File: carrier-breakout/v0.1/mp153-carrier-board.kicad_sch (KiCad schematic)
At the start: 85 parts, among them J1 USB-C_Receptacle_Molex_217179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, J10 3.5mm_Mono_Switched_sm, J11 3.5mm_Mono_Switched_sm, J12 3.5mm_Mono_Switched_sm, J13 3.5mm_Mono_Switched_sm, J2 Eurorack_Power_10pin_Shrouded, J6 Pins_02x40_P2.54mm_TH, J7 Pins_02x40_P2.54mm_TH, U11 TL072H, U12 TL072H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

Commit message: Laying out board - WIP
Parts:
- added JP1, JP10, JP11, JP12, JP13, JP14, JP15, JP2, JP3, JP4, JP5, JP6, JP7, JP8, JP9: SolderJumper_2_Open, 4ms_SolderJumper:JUMPER_SMD_1x2_tiny, symbol 4ms_Net_Tie:SolderJumper_2_Open
- added R1, R2: 10k_0402, 4ms_Resistor:R_0402, symbol 4ms_Resistor_0402:10k_0402
- J6, J7: footprint 4ms_Connector:Pins_2x40_P2.54mm_TH -> Connector_PinHeader_2.54mm:PinHeader_2x40_P2.54mm_Vertical
- R47, R48: value 4.7k_0402 -> 10k_0402; symbol 4ms_Resistor_0402:4.7k_0402 -> 4ms_Resistor_0402:10k_0402; Display 4.7k -> 10k; JLCPCB ID C105871 -> C60490; Part Number RC0402FR-074K7L -> RC0402FR-0710KL; Specifications 4.7k, 1%, 1/16W, 0402 -> 10k, 1%, 1/16W, 0402
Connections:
- net +3V3: now also JP12.2 (B), JP2.1 (A); no longer R47.2, R48.2
- net +5V: now also JP11.2 (B); no longer U3.3 (VDD), U3.4 (VDD)
- net +5VA: now also JP1.1 (A); no longer U9.24 (VCC)
- net A41: now also JP3.1 (A)
- net A43: now also JP4.1 (A)
- net A45: now also JP5.1 (A)
- net A47: now also JP6.1 (A)
- net A49: now also JP7.1 (A)
- net A51: now also JP8.1 (A)
- net A59: now also JP13.2 (B), JP9.1 (A)
- net A61: now also JP10.1 (A), JP14.2 (B)
- net A63: now also JP15.2 (B); no longer U3.5 (INT_N)
- net CODEC_RESET: now also JP3.2 (B)
- net I2C6_SCL: now also R48.2, JP10.2 (B); no longer R47.1, U3.6 (SCL)
- net I2C6_SDA: now also R47.1, JP9.2 (B); no longer R48.1, U3.7 (SDA)
- net SAI_FS: now also JP5.2 (B)
- net SAI_MCLK: now also JP4.2 (B)
- net SAI_SCK: now also JP6.2 (B)
- net SAI_SD_A: now also JP7.2 (B)
- net SAI_SD_B: now also JP8.2 (B)
- net 3v3_CODEC: now reaches C41.1, U9.7 (VDD)
- net 3v3_CODEC: now also R47.2, R48.1, JP2.2 (B)
- new net 3V3_FUSB: JP12.1 (A), R1.2, R2.2
- new net 5VA_CODEC: JP1.2 (B), U9.24 (VCC)
- new net 5V_FUSB: JP11.1 (A), U3.3 (VDD), U3.4 (VDD)
- new net FUSB_I2C6_SCL: JP14.1 (A), R2.1, U3.6 (SCL)
- new net FUSB_I2C6_SDA: JP13.1 (A), R1.1, U3.7 (SDA)
- new net FUSB_INT: JP15.1 (A), U3.5 (INT_N)
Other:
- moved on the sheet: C147, C148, C149, C150, C152, C153, C41, C42, C44, C45, C46, C48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

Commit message: Organized breakoutheader silk
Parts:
- J6, J7: footprint Connector_PinHeader_2.54mm:PinHeader_2x40_P2.54mm_Vertical -> 4ms_Connector:Pins_2x40_P2.54mm_TH

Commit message: WIP - completeing traces
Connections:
- net A71: now also L1.2; no longer L1.1
- net USBSW_5V: now also L1.1; no longer L1.2
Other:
- moved on the sheet: L1
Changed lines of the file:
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@@
 	(symbol
 		(lib_id "4ms_Inductor:FerriteBead_0603_0.8A_300mΩ")
-		(at 403.86 59.69 90)
+		(at 403.86 59.69 270)
+		(mirror x)
 		(unit 1)
 		(exclude_from_sim no)
@@
 		(dnp no)
 		(property "Reference" "L1"
-			(at 404.495 54.61 90)
+			(at 403.225 54.61 90)
 			(effects
 				(font
@@
 		)
 		(property "Footprint" "4ms_Resistor:R_0603"
-			(at 420.37 59.69 0)
+			(at 387.35 59.69 0)
 			(effects
 				(font
@@
 		)
 		(property "Datasheet" "https://datasheet.lcsc.com/lcsc/1811131631_TDK-MPZ1608S102ATA00_C76814.pdf"
-			(at 422.91 59.69 0)
+			(at 384.81 59.69 0)
 			(effects
 				(font
@@
 		)
 		(property "Manufacturer" "TDK"
-			(at 417.83 59.69 0)
+			(at 389.89 59.69 0)
 			(effects
 				(font
@@
 		)
 		(property "Part Number" "MPZ1608S102ATA00"
-			(at 415.29 57.15 0)
+			(at 392.43 57.15 0)
 			(effects
 				(font
@@
 		)
 		(property "Specifications" "Ferrite Bead 0.8A 300mΩ 0603"
-			(at 421.64 59.69 0)
+			(at 386.08 59.69 0)
 			(effects
 				(font
@@
 		)
 		(property "JLCPCB ID" "C76814"
-			(at 425.45 59.69 0)
+			(at 382.27 59.69 0)
 			(effects
 				(font
@@
 		)
 		(property "Production Stage" "A"
-			(at 420.37 62.23 0)
+			(at 387.35 62.23 0)
 			(effects
 				(font

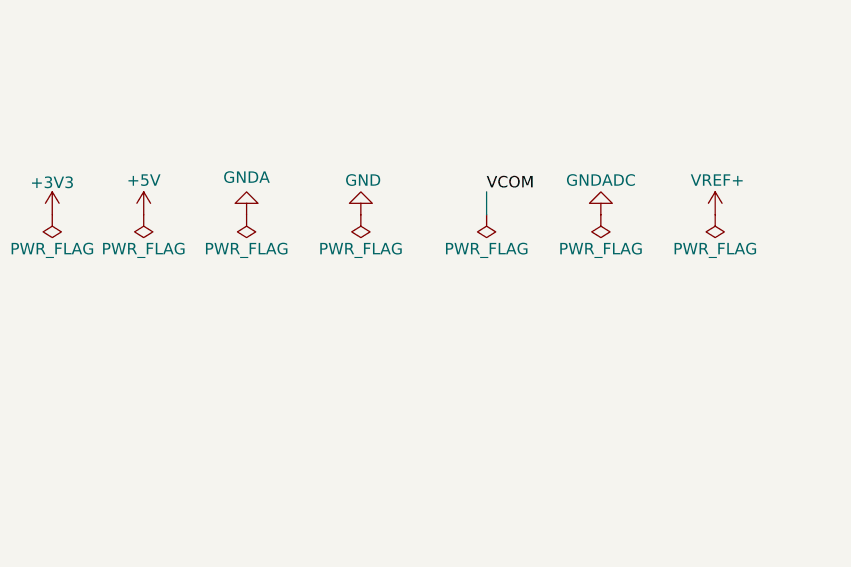
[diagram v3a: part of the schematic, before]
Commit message: Resolved ERC and DRC errors - warnings need to be reviewed. Cleaned up silk and cleaned up Audio out opamp section
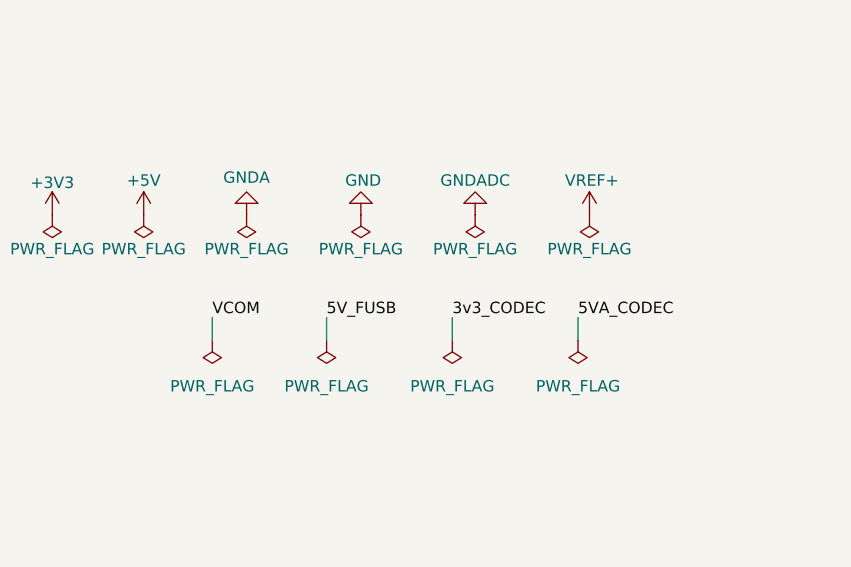
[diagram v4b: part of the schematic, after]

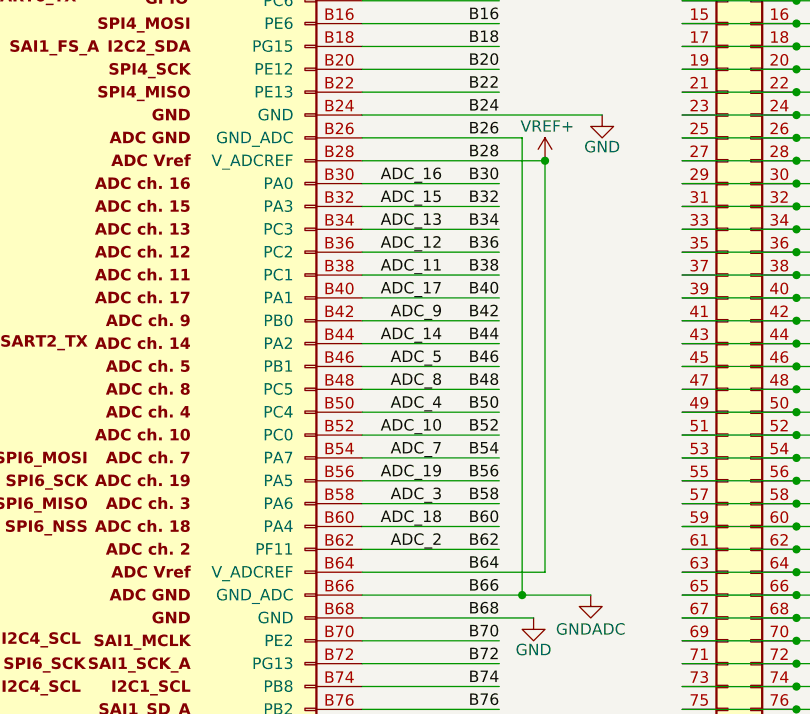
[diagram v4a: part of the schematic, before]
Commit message: Removed redundant ADC net labels
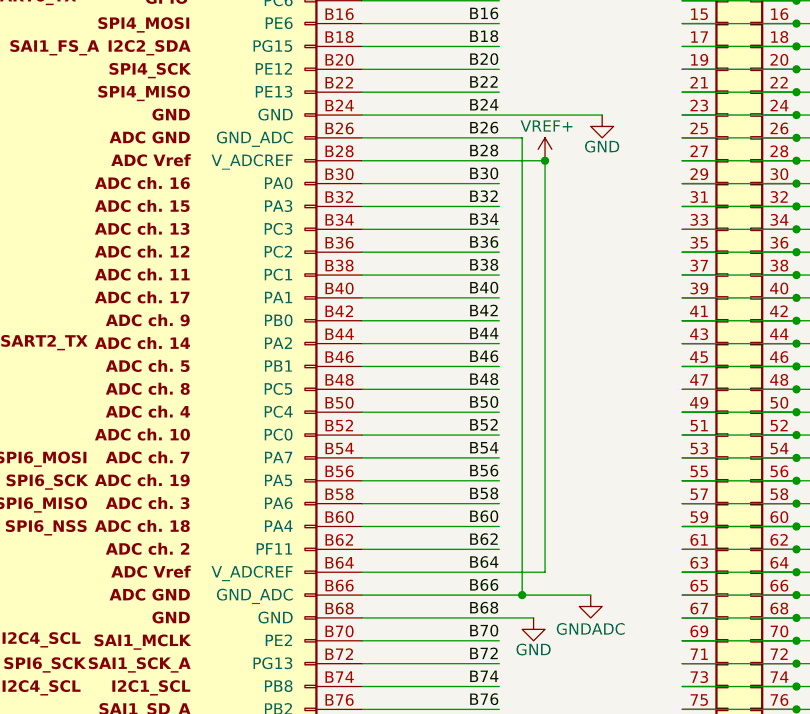
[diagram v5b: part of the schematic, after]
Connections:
- net ADC_10 renamed B52
- net ADC_11 renamed B38
- net ADC_12 renamed B36
- net ADC_13 renamed B34
- net ADC_14 renamed B44
- net ADC_15 renamed B32
- net ADC_16 renamed B30
- net ADC_17 renamed B40
- net ADC_18 renamed B60
- net ADC_19 renamed B56
- net ADC_2 renamed B62
- net ADC_3 renamed B58
- net ADC_4 renamed B50
- net ADC_5 renamed B46
- net ADC_7 renamed B54
- net ADC_8 renamed B48
- net ADC_9 renamed B42
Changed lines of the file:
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@@
-		)
-	)
-	(label "ADC_17"
-		(at 175.26 100.33 180)
-		(effects
-			(font
-				(size 1.27 1.27)
-			)
-			(justify right bottom)
-		)
-	)
-	(label "ADC_5"
-		(at 175.26 107.95 180)
-		(effects
-			(font
-				(size 1.27 1.27)
-			)
-			(justify right bottom)
 		)
 	)
@@
 		)
 	)
-	(label "ADC_11"
-		(at 175.26 97.79 180)
-		(effects
-			(font
-				(size 1.27 1.27)
-			)
-			(justify right bottom)
-		)
-	)
 	(label "B48"
 		(at 181.61 110.49 180)
@@
 		)
 	)
-	(label "ADC_19"
-		(at 175.26 120.65 180)
-		(effects
-			(font
-				(size 1.27 1.27)
-			)
-			(justify right bottom)
-		)
-	)
-	(label "ADC_4"
-		(at 175.26 113.03 180)
-		(effects
-			(font
-				(size 1.27 1.27)
-			)
-			(justify right bottom)
-		)
-	)
 	(label "B10"
 		(at 181.61 62.23 180)
@@
 		)
 	)
-	(label "ADC_16"
-		(at 175.26 87.63 180)
-		(effects
-			(font
-				(size 1.27 1.27)
-			)
-			(justify right bottom)
-		)
-	)
 	(label "VCOM"
 		(at 450.85 300.99 0)
@@
 		)
 	)
-	(label "ADC_15"
-		(at 175.26 90.17 180)
-		(effects
-			(font
-				(size 1.27 1.27)
-			)
-			(justify right bottom)
-		)
-	)
 	(label "B24"
 		(at 223.52 80.01 180)
@@
 		)
 	)
-	(label "ADC_7"
-		(at 175.26 118.11 180)
-		(effects
-			(font
-				(size 1.27 1.27)
-			)
-			(justify right bottom)
-		)
-	)
 	(label "A55"
 		(at 59.69 120.65 0)
@@
 		)
 	)
-	(label "ADC_2"
-		(at 175.26 128.27 180)
-		(effects
-			(font
-				(size 1.27 1.27)
-			)
-			(justify right bottom)
-		)
-	)
 	(label "A61"
 		(at 25.4 127 0)
@@
 		)
 	)
-	(label "ADC_10"
-		(at 175.26 115.57 180)
-		(effects
-			(font
-				(size 1.27 1.27)
-			)
-			(justify right bottom)
-		)
-	)
 	(label "USB_HS_D-"
 		(at 64.77 148.59 0)
@@
 		)
 	)
-	(label "ADC_8"
-		(at 175.26 110.49 180)
-		(effects
-			(font
-				(size 1.27 1.27)
-			)
-			(justify right bottom)
-		)
-	)
 	(label "B2"
 		(at 181.61 52.07 180)
@@
 		)
 	)
-	(label "ADC_12"
-		(at 175.26 95.25 180)
-		(effects
-			(font
-				(size 1.27 1.27)
-			)
-			(justify right bottom)
-		)
-	)
 	(label "A11"
 		(at 59.69 64.77 0)
@@
 		)
 	)
-	(label "ADC_9"
-		(at 175.26 102.87 180)
-		(effects
-			(font
-				(size 1.27 1.27)
-			)
-			(justify right bottom)
-		)
-	)
 	(label "A43"
 		(at 59.69 105.41 0)
@@
 		)
 	)
-	(label "ADC_3"
-		(at 175.26 123.19 180)
-		(effects
-			(font
-				(size 1.27 1.27)
-			)
-			(justify right bottom)
-		)
-	)
 	(label "VCOM"
 		(at 238.76 260.35 0)
@@
 		)
 	)
-	(label "ADC_18"
-		(at 175.26 125.73 180)
-		(effects
-			(font
-				(size 1.27 1.27)
-			)
-			(justify right bottom)
-		)
-	)
 	(label "A73"
 		(at 59.69 143.51 0)
@@
 		)
 	)
-	(label "ADC_13"
-		(at 175.26 92.71 180)
-		(effects
-			(font
-				(size 1.27 1.27)
-			)
-			(justify right bottom)
-		)
-	)
 	(label "SAI_SCK"
 		(at 151.13 278.13 180)
@@
 		(effects
 			(font
-				(size 1.27 1.27)
-			)
-			(justify right bottom)
-		)
-	)
-	(label "ADC_14"
-		(at 175.26 105.41 180)
-		(effects
-			(font

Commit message: carrier-breakout cleanup:
- Fix nets with two names
- Fix some silk overlap DRC warning for components too close
- Add more space for pins names to fix DRC warnings for silk sizes
- Remove empty boxes on silk
- Space out jumpers that we may have to cut with an exacto (more space = easier to cut)
- Added jumper for USB_5V_ENABLE, and pull-down to prevent floating when jumper is cut
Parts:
- removed C70: 4.7uF_0402_6.3V, 4ms_Capacitor:C_0402, symbol 4ms_Capacitor:4.7uF_0402_6.3V
- added JP16: SolderJumper_2_Open, 4ms_SolderJumper:JUMPER_SMD_1x2_tiny, symbol 4ms_Net_Tie:SolderJumper_2_Open
- added R3: 10k_0402, 4ms_Resistor:R_0402, symbol 4ms_Resistor_0402:10k_0402
- C11, C3, C41, C45: value 100nF_0402_16V -> 100nF_0402_50V; symbol 4ms_Capacitor:100nF_0402_16V -> 4ms_Capacitor:100nF_0402_50V
- C74: value 22uF_1206_25V -> 22uF_0805_25V; symbol 4ms_Capacitor:22uF_1206_25V -> 4ms_Capacitor:22uF_0805_25V
- U13: Manufacturer 2 Diodes Inc -> (none); Manufacturer 3 Diodes Inc -> (none); Part Number 2 AP62300Z6 -> (none); Part Number 3 AP62300TZ6 -> (none)
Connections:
- net A57: now also JP16.2 (B); no longer U14.3 (EN)
- net GND: now also R3.1
- net A71 renamed USB_VBUS_JACK
- net A75 renamed USB_HS_D+
- net A77 renamed USB_HS_D-
- new net USB_5V_ENABLE: JP16.1 (A), R3.2, U14.3 (EN)
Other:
- note added: "A21"
- note added: "A23"
- note added: "A25"
- note added: "A27"
- note added: "A29"
- note added: "A31"
- note added: "A33"
- note added: "A35"
- note added: "A37"
- note added: "A53"
- note added: "A65"
- note added: "A67"
- note added: "A69"
- note added: "A71"
- note added: "A73"
- note added: "A75"
- note added: "A77"
- note added: "A79"
- note added: "B24"
- note added: "B26"
- note added: "B28"
- note added: "B64"
- note added: "B66"
- note added: "B68"
- note added: "B78"
- note added: "B80"
- note added: "Breakout carrier board for mp153-devboard v0.2"
- note removed: "Example carrier board for mp153-devboard v0.3"
- moved on the sheet: J6
